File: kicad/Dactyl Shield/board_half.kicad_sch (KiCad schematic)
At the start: 43 parts, among them J301 JST, J302 Split, J303 Column, J304 Thumb, J305 External, J306 Row, J307 Display, J308 Vic, J309 ResA, J312 ResB, Q301 AO3400A, SW301 Battery, SW302 Reset, SW303 LED, U301 SRV05-4, U302 Nice!Nano/2040

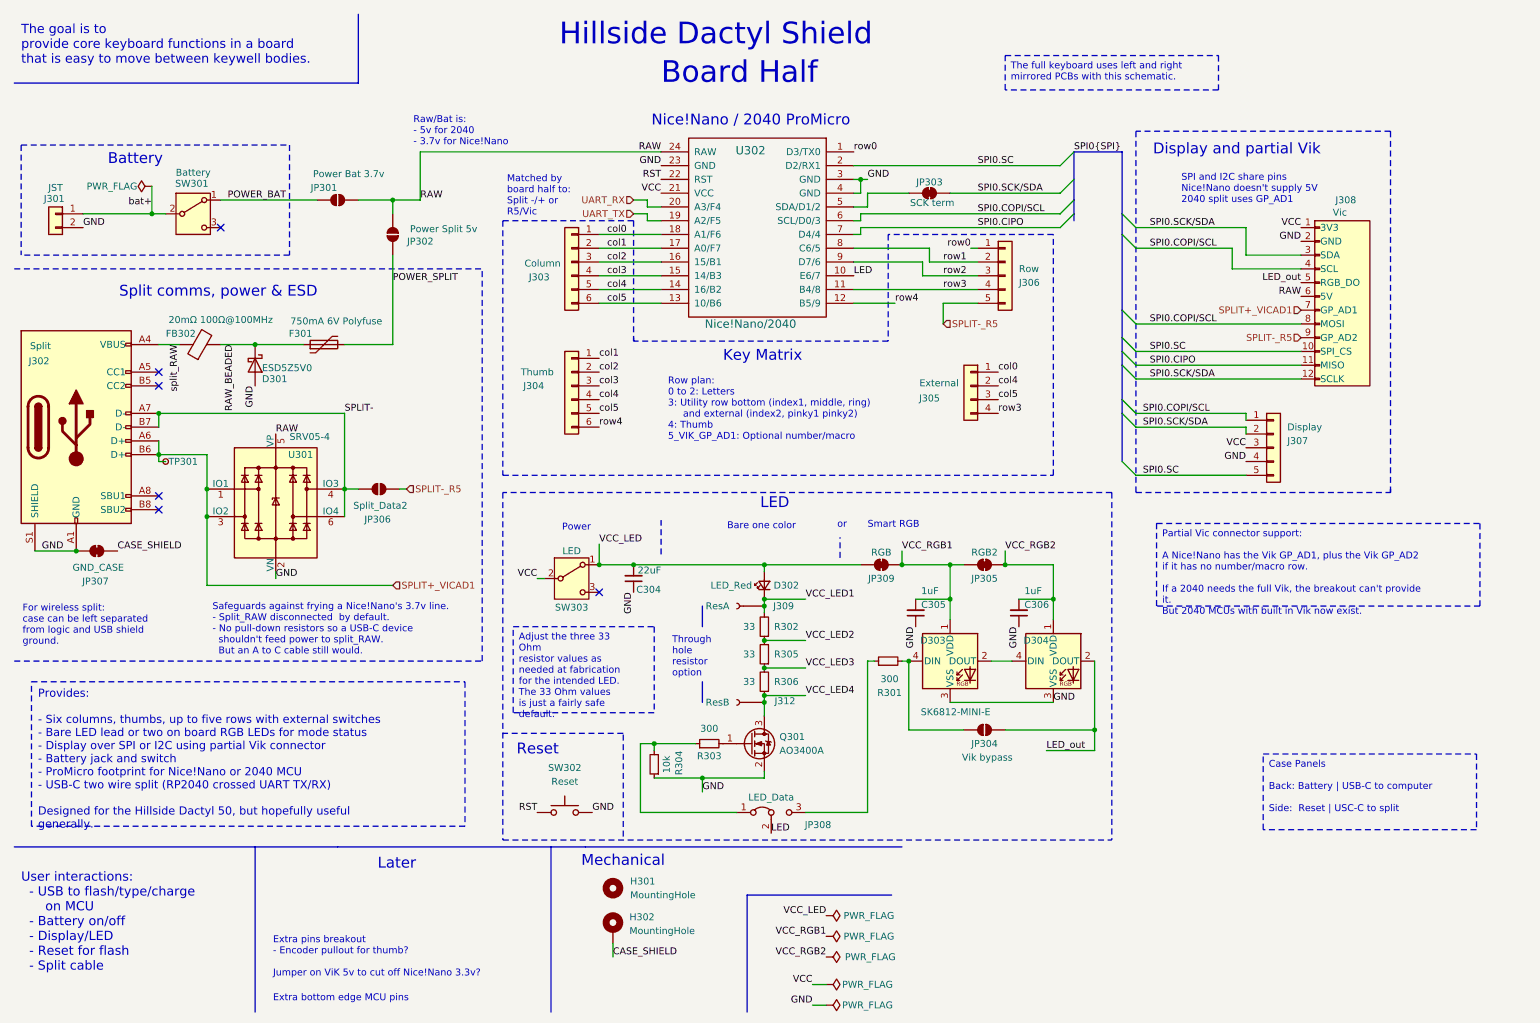
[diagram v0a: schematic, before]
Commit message: refactor: cleanup schematic; external -> foot
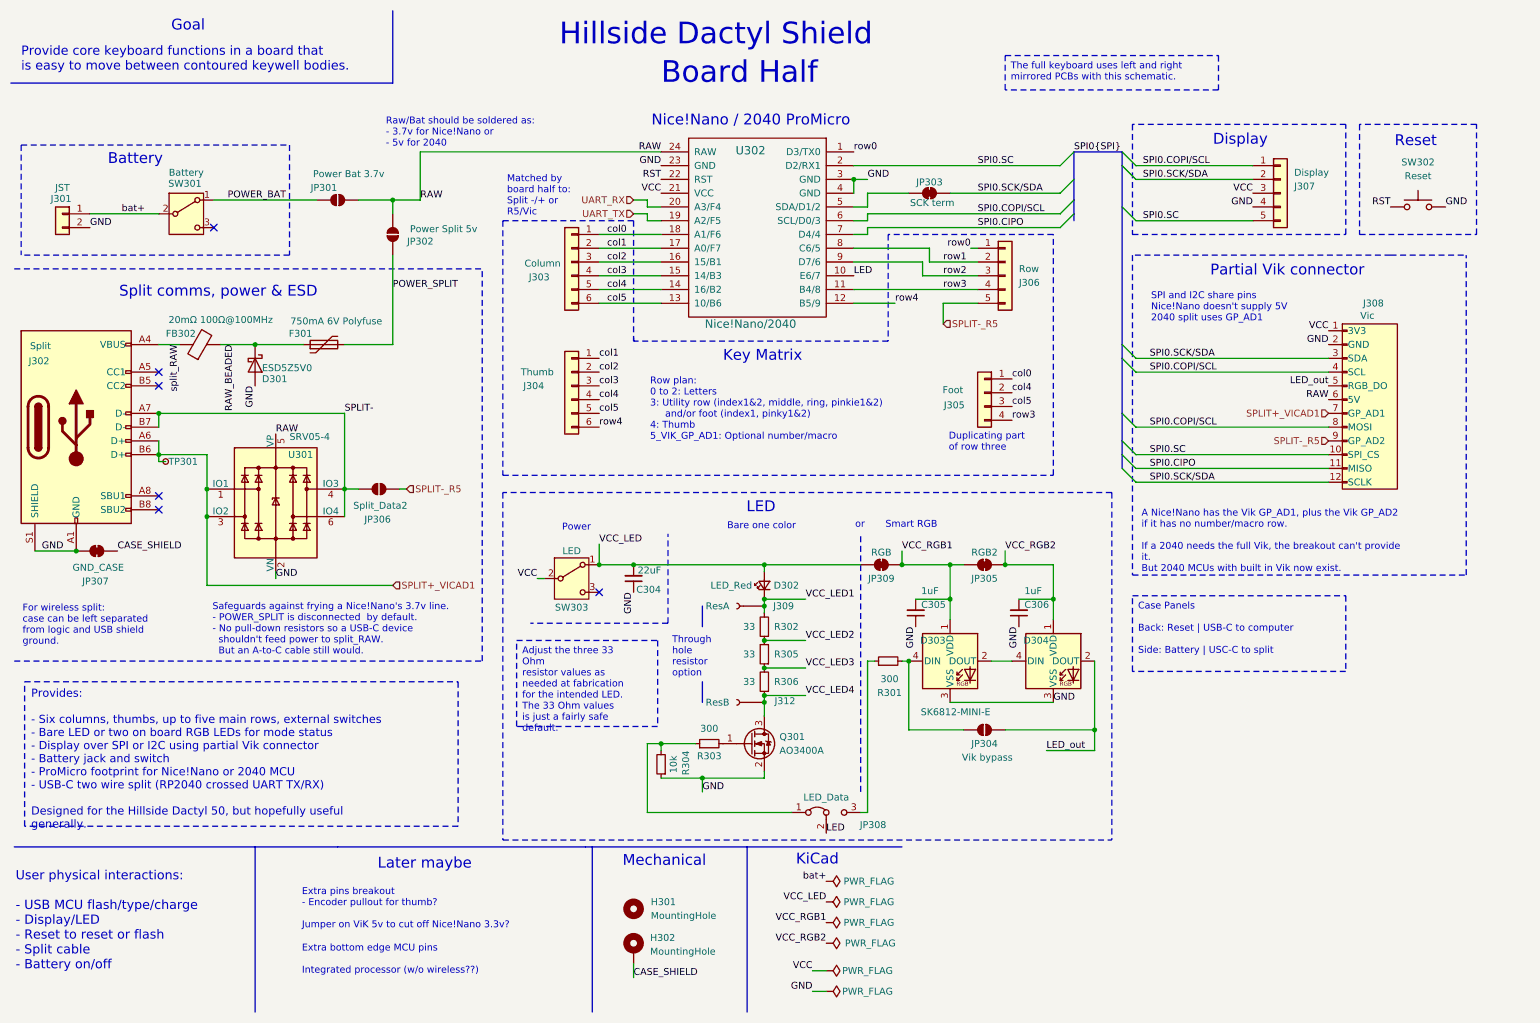
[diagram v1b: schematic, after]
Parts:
- J305: value External -> Foot
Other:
- note added: "Display"
- note added: "Duplicating part of row three"
- note added: "Extra bottom edge MCU pins Integrated processor (w/o wireless??)"
- note added: "Goal"
- note added: "KiCad"
- note added: "Later maybe"
- note added: "Partial Vik connector"
- note added: "Provide core keyboard functions in a board that is easy to move between contoured keywell bodies."
- note added: "Raw/Bat should be soldered as: - 3.7v for Nice!Nano or - 5v for 2040"
- note added: "Row plan: 0 to 2: Letters 3: Utility row (index1&2, middle, ring, pinkie1&2) and/or foot (index1, pinky1&2) 4: Thumb 5_VIK_GP_AD1: Optional number/macro"
- note added: "Safeguards against frying a Nice!Nano's 3.7v line. - POWER_SPLIT is disconnected by default. - No pull-down resistors so a USB-C device shouldn't feed power to split_RAW. But an A-to-C cable still would."
- note added: "User physical interactions: - USB MCU flash/type/charge - Display/LED - Reset to reset or flash - Split cable - Battery on/off"
- note removed: "Display and partial Vik"
- note removed: "Extra bottom edge MCU pins"
- note removed: "Later"
- note removed: "Raw/Bat is: - 5v for 2040 - 3.7v for Nice!Nano"
- note removed: "Row plan: 0 to 2: Letters 3: Utility row bottom (index1, middle, ring) and external (index2, pinky1 pinky2) 4: Thumb 5_VIK_GP_AD1: Optional number/macro"
- note removed: "Safeguards against frying a Nice!Nano's 3.7v line. - Split_RAW disconnected by default. - No pull-down resistors so a USB-C device shouldn't feed power to split_RAW. But an A to C cable still would."
- note removed: "The goal is to provide core keyboard functions in a board that is easy to move between keywell bodies."
- note removed: "User interactions: - USB to flash/type/charge on MCU - Battery on/off - Display/LED - Reset for flash - Split cable"
- moved on the sheet: H301, H302, J301, J305, J307, J308, JP308, R304, SW301, SW302

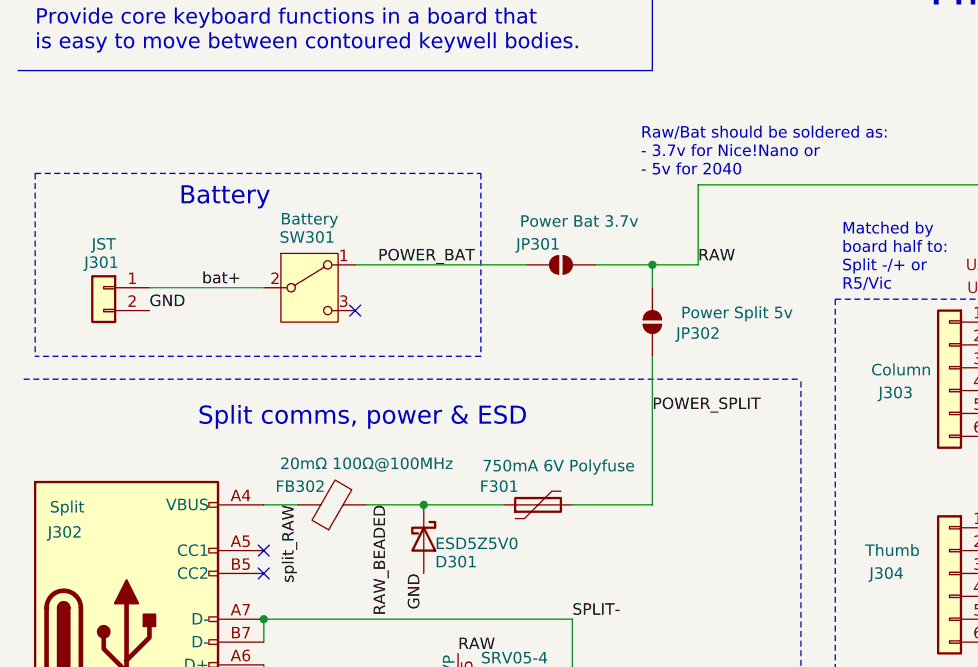
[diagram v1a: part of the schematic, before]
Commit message: feat: reset on back, power slides to right
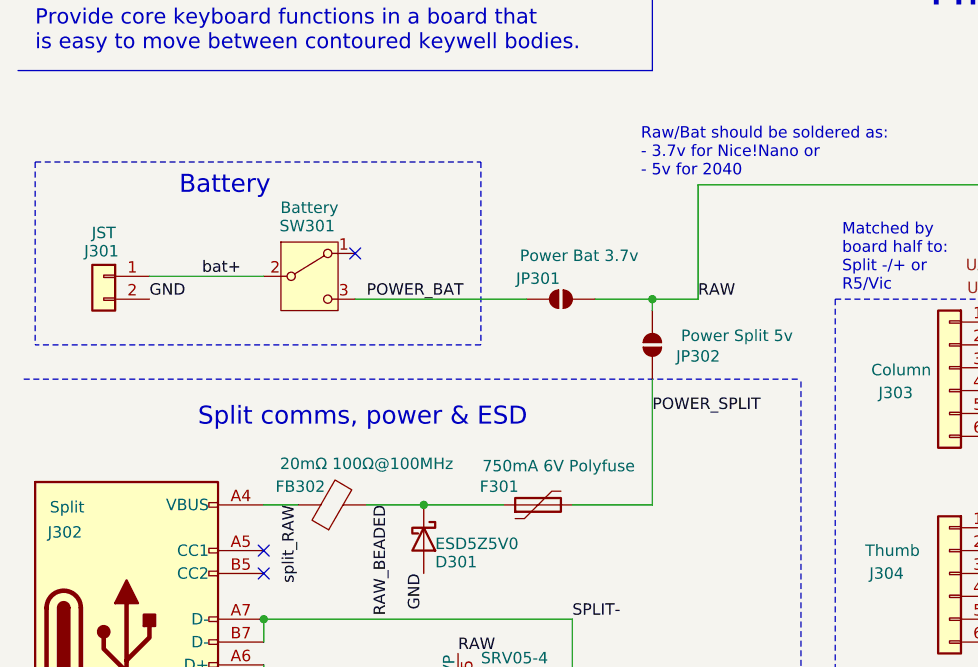
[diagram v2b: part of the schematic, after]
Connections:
- net POWER_BAT: now also SW301.3 (C); no longer SW301.1 (A)
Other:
- moved on the sheet: J301, JP301, JP302, SW301
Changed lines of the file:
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@@
 	)
 	(junction
-		(at 82.55 46.99)
-		(diameter 0)
-		(color 0 0 0 0)
-	)
-	(junction
 		(at 24.13 111.76)
 		(diameter 0)
@@
 	)
 	(junction
+		(at 82.55 50.8)
+		(diameter 0)
+		(color 0 0 0 0)
+	)
+	(junction
 		(at 151.13 120.65)
 		(diameter 0)
@@
 	)
 	(no_connect
-		(at 49.53 52.07)
+		(at 49.53 45.72)
 	)
 	(no_connect
@@
 	(wire
 		(pts
-			(xy 76.2 46.99) (xy 82.55 46.99)
+			(xy 76.2 50.8) (xy 82.55 50.8)
 		)
 		(stroke
@@
 	(wire
 		(pts
-			(xy 82.55 46.99) (xy 82.55 49.53)
+			(xy 82.55 50.8) (xy 82.55 52.07)
 		)
 		(stroke
@@
 	(wire
 		(pts
-			(xy 49.53 46.99) (xy 68.58 46.99)
-		)
-		(stroke
-			(width 0)
-			(type default)
-		)
-	)
-	(wire
-		(pts
 			(xy 195.58 114.3) (xy 204.47 114.3)
 		)
@@
 	(wire
 		(pts
-			(xy 87.63 38.1) (xy 87.63 46.99)
+			(xy 87.63 38.1) (xy 87.63 50.8)
 		)
 		(stroke
@@
 	(wire
 		(pts
-			(xy 87.63 46.99) (xy 82.55 46.99)
+			(xy 87.63 50.8) (xy 82.55 50.8)
 		)
 		(stroke
@@
 	(wire
 		(pts
-			(xy 82.55 57.15) (xy 82.55 73.66)
+			(xy 49.53 50.8) (xy 68.58 50.8)
+		)
+		(stroke
+			(width 0)
+			(type default)
+		)
+	)
+	(wire
+		(pts
+			(xy 82.55 59.69) (xy 82.55 73.66)
 		)
 		(stroke
@@
 	(polyline
 		(pts
-			(xy 13.97 36.83) (xy 13.97 57.15)
+			(xy 13.97 35.56) (xy 13.97 55.88)
 		)
 		(stroke
@@
 	(polyline
 		(pts
-			(xy 63.5 36.83) (xy 63.5 57.15)
+			(xy 63.5 35.56) (xy 63.5 55.88)
 		)
 		(stroke
@@
 	(polyline
 		(pts
-			(xy 13.97 36.83) (xy 63.5 36.83)
+			(xy 13.97 35.56) (xy 63.5 35.56)
 		)
 		(stroke
@@
 	(wire
 		(pts
-			(xy 26.67 49.53) (xy 39.37 49.53)
+			(xy 26.67 48.26) (xy 39.37 48.26)
 		)
 		(stroke
@@
 	(polyline
 		(pts
-			(xy 63.5 57.15) (xy 13.97 57.15)
+			(xy 63.5 55.88) (xy 13.97 55.88)
 		)
 		(stroke
@@
 	(text "Battery"
 		(exclude_from_sim no)
-		(at 29.972 40.64 0)
+		(at 29.972 39.37 0)
 		(effects
 			(font
@@
 	)
 	(label "GND"
-		(at 26.67 52.07 0)
+		(at 26.67 50.8 0)
 		(effects
 			(font
@@
 	)
 	(label "RAW"
-		(at 87.63 46.99 0)
+		(at 87.63 50.8 0)
 		(effects
 			(font
@@
 	)
 	(label "bat+"
-		(at 36.83 49.53 180)
+		(at 36.83 48.26 180)
 		(effects
 			(font
@@
 	)
 	(label "POWER_BAT"
-		(at 52.07 46.99 0)
+		(at 50.8 50.8 0)
 		(effects
 			(font
@@
 	(symbol
 		(lib_id "Switch:SW_SPDT")
-		(at 44.45 49.53 0)
+		(at 44.45 48.26 0)
 		(unit 1)
 		(exclude_from_sim no)
@@
 		(dnp no)
 		(property "Reference" "SW301"
-			(at 44.196 43.942 0)
+			(at 44.196 42.672 0)
 			(effects
 				(font
@@
 		)
 		(property "Value" "Battery"
-			(at 44.45 41.91 0)
+			(at 44.45 40.64 0)
 			(effects
 				(font
@@
 		)
 		(property "Footprint" "Dactyl:SW_SPDT_Battery"
-			(at 44.45 49.53 0)
+			(at 44.45 48.26 0)
 			(effects
 				(font
@@
 		)
 		(property "Datasheet" "~"
-			(at 44.45 57.15 0)
+			(at 44.45 55.88 0)
 			(effects
 				(font
@@
 		)
 		(property "Description" ""
-			(at 44.45 49.53 0)
+			(at 44.45 48.26 0)
 			(effects
 				(font
@@
 		)
 		(property "JLC PCBA Type" "Standard"
-			(at 44.45 49.53 0)
+			(at 44.45 48.26 0)
 			(effects
 				(font
@@
 		)
 		(property "Config" ""
-			(at 44.45 49.53 0)
+			(at 44.45 48.26 0)
 			(effects
 				(font
@@
 		)
 		(property "LCSC Part" "C221662"
-			(at 44.45 49.53 0)
+			(at 44.45 48.26 0)
 			(effects
 				(font
@@
 		)
 		(property "Role" "Batt"
-			(at 44.45 49.53 0)
+			(at 44.45 48.26 0)
 			(effects
 				(font
@@
 		)
 		(property "Sim.Device" ""
-			(at 44.45 49.53 0)
+			(at 44.45 48.26 0)
 			(effects
 				(font
@@
 		)
 		(property "Sim.Pins" ""
-			(at 44.45 49.53 0)
+			(at 44.45 48.26 0)
 			(effects
 				(font
@@
 	(symbol
 		(lib_id "Connector_Generic:Conn_01x02")
-		(at 21.59 49.53 0)
+		(at 21.59 48.26 0)
 		(mirror y)
 		(unit 1)
@@
 		(dnp no)
 		(property "Reference" "J301"
-			(at 21.336 46.736 0)
+			(at 21.336 45.466 0)
 			(effects
 				(font
@@
 		)
 		(property "Value" "JST"
-			(at 21.59 44.704 0)
+			(at 21.59 43.434 0)
 			(effects
 				(font
@@
 		)
 		(property "Footprint" "Dactyl:JST_PH_S2B-PH-K_1x02_P2.00mm_Horizontal"
-			(at 21.59 49.53 0)
+			(at 21.59 48.26 0)
 			(effects
 				(font
@@
 		)
 		(property "Datasheet" "~"
-			(at 21.59 49.53 0)
+			(at 21.59 48.26 0)
 			(effects
 				(font
@@
 		)
 		(property "Description" "Generic connector, single row, 01x02, script generated (kicad-library-utils/schlib/autogen/connector/)"
-			(at 21.59 49.53 0)
+			(at 21.59 48.26 0)
 			(effects
 				(font
@@
 		)
 		(property "Config" "DNF"
-			(at 21.59 49.53 0)
+			(at 21.59 48.26 0)
 			(effects
 				(font
@@
 		)
 		(property "Role" "Battery"
-			(at 21.59 49.53 0)
+			(at 21.59 48.26 0)
 			(effects
 				(font
@@
 		)
 		(property "Sim.Device" ""
-			(at 21.59 49.53 0)
+			(at 21.59 48.26 0)
 			(effects
 				(font
@@
 		)
 		(property "Sim.Pins" ""
-			(at 21.59 49.53 0)
+			(at 21.59 48.26 0)
 			(effects
 				(font
@@
 	(symbol
 		(lib_id "Jumper:SolderJumper_2_Open")
-		(at 72.39 46.99 0)
+		(at 72.39 50.8 0)
 		(unit 1)
 		(exclude_from_sim yes)
@@
 		(dnp no)
 		(property "Reference" "JP301"
-			(at 69.85 44.704 0)
+			(at 69.85 48.514 0)
 			(effects
 				(font
@@
 		)
 		(property "Value" "Power Bat 3.7v"
-			(at 74.422 42.164 0)
+			(at 74.422 45.974 0)
 			(effects
 				(font
@@
 		)
 		(property "Footprint" "Dactyl_basics:SolderJumper-2_P1.3mm_Open_RoundedPad1.0x1.5mm"
-			(at 72.39 46.99 0)
+			(at 72.39 50.8 0)
 			(effects
 				(font
@@
 		)
 		(property "Datasheet" "~"
-			(at 72.39 46.99 0)
+			(at 72.39 50.8 0)
 			(effects
 				(font
@@
 		)
 		(property "Description" "Solder Jumper, 2-pole, open"
-			(at 72.39 46.99 0)
+			(at 72.39 50.8 0)
 			(effects
 				(font
@@
 		)
 		(property "Config" "DNF"
-			(at 72.39 46.99 0)
+			(at 72.39 50.8 0)
 			(effects
 				(font
@@
 		)
 		(property "Role" "Power"
-			(at 72.39 46.99 0)
+			(at 72.39 50.8 0)
 			(effects
 				(font
@@
 		)
 		(property "Sim.Device" ""
-			(at 72.39 46.99 0)
+			(at 72.39 50.8 0)
 			(effects
 				(font
@@
 		)
 		(property "Sim.Pins" ""
-			(at 72.39 46.99 0)
+			(at 72.39 50.8 0)
 			(effects
 				(font
@@
 		(lib_name "SolderJumper_2_Open_1")
 		(lib_id "Jumper:SolderJumper_2_Open")
-		(at 82.55 53.34 90)
+		(at 82.55 55.88 90)
 		(unit 1)
 		(exclude_from_sim yes)
@@
 		(dnp no)
 		(property "Reference" "JP302"
-			(at 87.63 54.61 90)
+			(at 87.63 57.15 90)
 			(effects
 				(font
@@
 		)
 		(property "Value" "Power Split 5v"
-			(at 91.948 52.324 90)
+			(at 91.948 54.864 90)
 			(effects
 				(font
@@
 		)
 		(property "Footprint" "Dactyl_basics:SolderJumper-2_P1.3mm_Open_RoundedPad1.0x1.5mm"
-			(at 82.55 53.34 0)
+			(at 82.55 55.88 0)
 			(effects
 				(font
@@
 		)
 		(property "Datasheet" "~"
-			(at 82.55 53.34 0)
+			(at 82.55 55.88 0)
 			(effects
 				(font
@@
 		)
 		(property "Description" "Solder Jumper, 2-pole, open"
-			(at 82.55 53.34 0)
+			(at 82.55 55.88 0)
 			(effects
 				(font
@@
 		)
 		(property "Config" "DNF"
-			(at 82.55 53.34 0)
+			(at 82.55 55.88 0)
 			(effects
 				(font
@@
 		)
 		(property "Role" "Power"
-			(at 82.55 53.34 0)
+			(at 82.55 55.88 0)
 			(effects
 				(font
@@
 		)
 		(property "Sim.Device" ""
-			(at 82.55 53.34 0)
+			(at 82.55 55.88 0)
 			(effects
 				(font
@@
 		)
 		(property "Sim.Pins" ""
-			(at 82.55 53.34 0)
+			(at 82.55 55.88 0)
 			(effects
 				(font

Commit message: feat: use open solder jumpers to LEDs
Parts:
- removed JP308: LED_Data, Jumper:SolderJumper-3_P1.3mm_Bridged12_RoundedPad1.0x1.5mm, symbol Jumper:Jumper_3_Bridged12
- added JP208: LED_DATA, Jumper:SolderJumper-3_P1.3mm_Open_RoundedPad1.0x1.5mm, symbol Jumper:SolderJumper_3_Open
- JP205: renamed from JP305; footprint Dactyl_basics:SolderJumper-2_P1.3mm_Bridged_RoundedPad1.0x1.5mm -> Dactyl_basics:SolderJumper-2_P1.3mm_Open_RoundedPad1.0x1.5mm; symbol Jumper:SolderJumper_2_Bridged -> Jumper:SolderJumper_2_Open
- JP209: renamed from JP309; footprint Dactyl_basics:SolderJumper-2_P1.3mm_Bridged_RoundedPad1.0x1.5mm -> Dactyl_basics:SolderJumper-2_P1.3mm_Open_RoundedPad1.0x1.5mm; symbol Jumper:SolderJumper_2_Bridged -> Jumper:SolderJumper_2_Open
- renumbered C304 to C204, C305 to C205, C306 to C206, D301 to D201, D302 to D202, D303 to D203, D304 to D204, F301 to F201, FB302 to FB202, H301 to H201, H302 to H202, J301 to J201, J302 to J202, J303 to J203, J304 to J204, J305 to J205, J306 to J206, J307 to J207, J308 to J208, J309 to J209, J312 to J212, JP301 to JP201, JP302 to JP202, JP303 to JP203, JP304 to JP204, JP306 to JP206, JP307 to JP207, Q301 to Q201, R301 to R201, R302 to R202, R303 to R203, R304 to R204, R305 to R205, R306 to R206, SW301 to SW201, SW302 to SW202, SW303 to SW203, TP301 to TP201, U301 to U201, U302 to U202
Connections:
- net LED: now also JP208.2 (C)
- net at R203.1, R204.2: now also JP208.1 (A)
- net at R201.1: now also JP208.3 (B)
